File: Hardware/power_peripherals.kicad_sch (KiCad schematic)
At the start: 46 parts, among them J10 microSD_Friction, J11 Qwiic_RA, J5 Conn_01x10, J6 Conn_01x10, J7 Conn_01x10, J8 Conn_01x10, J9 JST_2mm_LiPo, Q1 DMG2305UX, SW2 SMD_4.6x2.8mm_h2.5mm, SW3 SMD_4.6x2.8mm_h2.5mm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

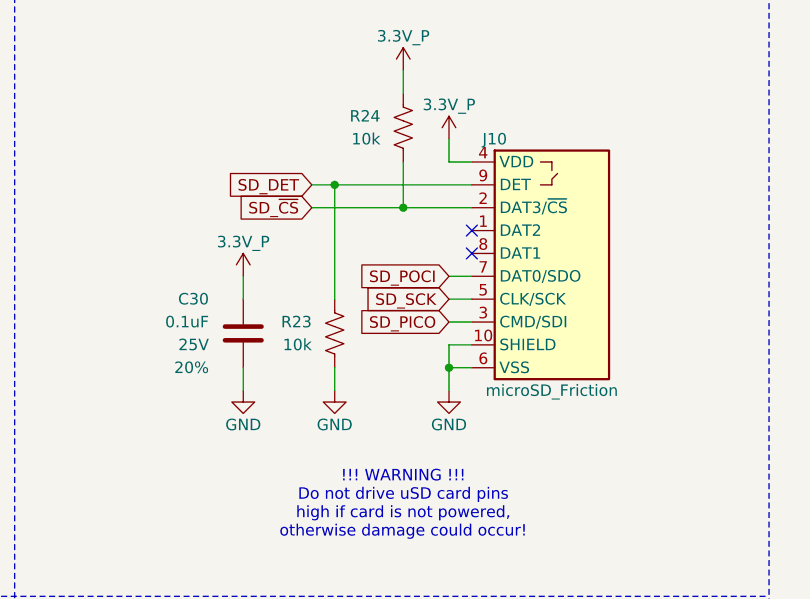
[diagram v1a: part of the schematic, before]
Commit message: Symbol and footprint update
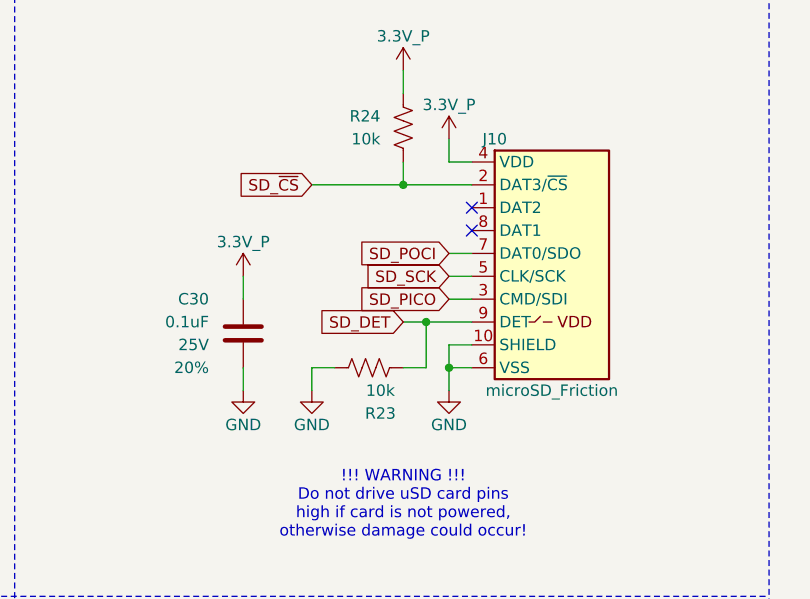
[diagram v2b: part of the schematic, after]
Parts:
- D4: footprint SparkFun-LED:WS2812-2020 -> SparkFun-LED:WS2812_2020
- J10: footprint SparkFun-Connector:microSD_Friction_Fit_Atom -> SparkFun-Connector:microSD_Friction_Fit_Common
- SW2, SW3, SW4: footprint SparkFun-Switch:Push_SMD_4.6x2.8mm -> SparkFun-Switch:Push_SMD_4.6x2.8mm_h2.5mm
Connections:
- net at J11.NC1 (NC): no longer J11.NC2 (NC)
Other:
- moved on the sheet: R23

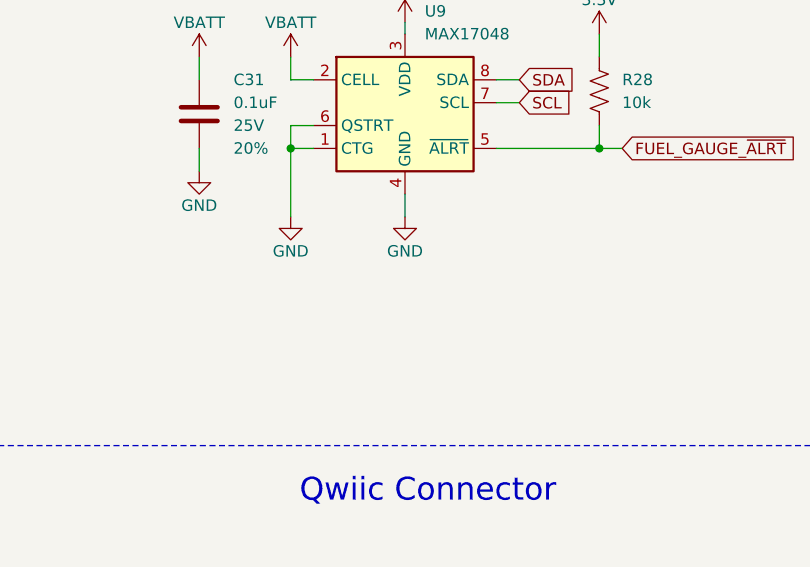
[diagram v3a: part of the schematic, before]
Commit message: Checklist update
Update 1.4A inductor
Update date design
Add I2C address of fuel gauge
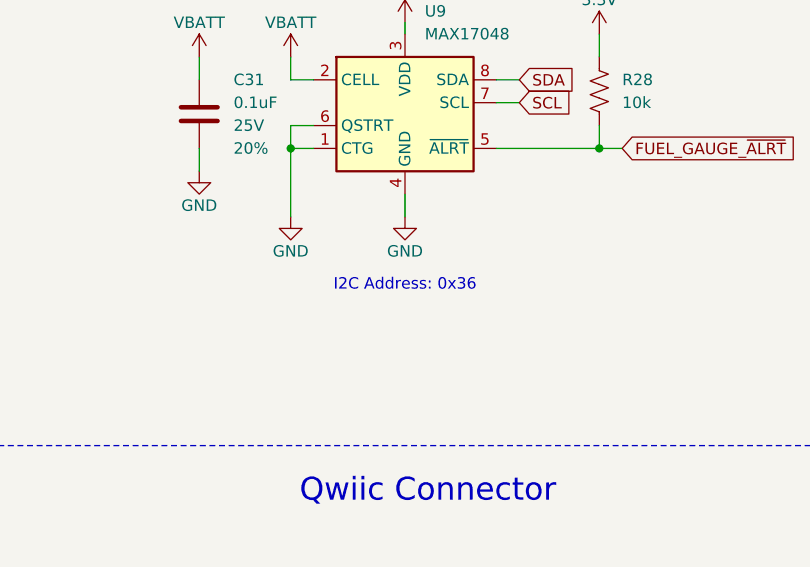
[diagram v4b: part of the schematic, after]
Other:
- note added: "I2C Address: 0x36"
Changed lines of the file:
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@@
 	(title_block
 		(title "SparkFun IoT Node - LoRaWAN")
-		(date "2024-10-24")
+		(date "2024-11-04")
 		(rev "v10")
 		(company "SparkFun")
@@
 			)
 		)
+	)
+	(text "I2C Address: 0x36"
+		(exclude_from_sim no)
+		(at 368.3 83.82 0)
+		(effects
+			(font
+				(size 1.27 1.27)
+			)
+		)

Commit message: Library update
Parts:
- D5: footprint SparkFun-LED:LED_0603_1608Metric -> SparkFun-LED:LED_0603_1608Metric_Red
- D6: footprint SparkFun-LED:LED_0603_1608Metric -> SparkFun-LED:LED_0603_1608Metric_Yellow
- U7: IMax (none) -> 600mA; VMax 6V -> 5.5V
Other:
- note removed: "Max input voltage: 5.5V Max curret output: 600mA"
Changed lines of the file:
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@@
 		)
 	)
-	(text "Max input voltage: 5.5V\nMax curret output: 600mA"
-		(exclude_from_sim no)
-		(at 91.44 53.34 0)
-		(effects
-			(font
-				(size 1.27 1.27)
-			)
-		)
-	)
 	(global_label "XBLR_IO2"
 		(shape input)
@@
 			)
 		)
-		(property "Footprint" "SparkFun-LED:LED_0603_1608Metric"
+		(property "Footprint" "SparkFun-LED:LED_0603_1608Metric_Red"
 			(at 217.17 229.87 0)
 			(effects
@@
 			)
 		)
-		(property "Footprint" "SparkFun-LED:LED_0603_1608Metric"
+		(property "Footprint" "SparkFun-LED:LED_0603_1608Metric_Yellow"
 			(at 211.074 69.85 0)
 			(effects
@@
 		(fields_autoplaced yes)
 		(property "Reference" "U7"
-			(at 91.44 57.15 0)
+			(at 91.44 52.07 0)
 			(effects
 				(font
@@
 		)
 		(property "Value" "RT9080-3.3"
-			(at 91.44 59.69 0)
+			(at 91.44 54.61 0)
 			(effects
 				(font
@@
 			)
 		)
-		(property "VMax" "6V"
-			(at 91.44 85.09 0)
+		(property "VMax" "5.5V"
+			(at 91.44 57.15 0)
+			(show_name yes)
 			(effects
 				(font
 					(size 1.27 1.27)
 				)
-				(hide yes)
 			)
 		)
@@
 			)
 		)
+		(property "IMax" "600mA"
+			(at 91.44 59.69 0)
+			(show_name yes)
+			(effects
+				(font
+					(size 1.27 1.27)
+				)
+			)
+		)
